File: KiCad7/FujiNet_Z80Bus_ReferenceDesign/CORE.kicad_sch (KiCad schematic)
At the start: 16 parts, among them IC1 74HC32N

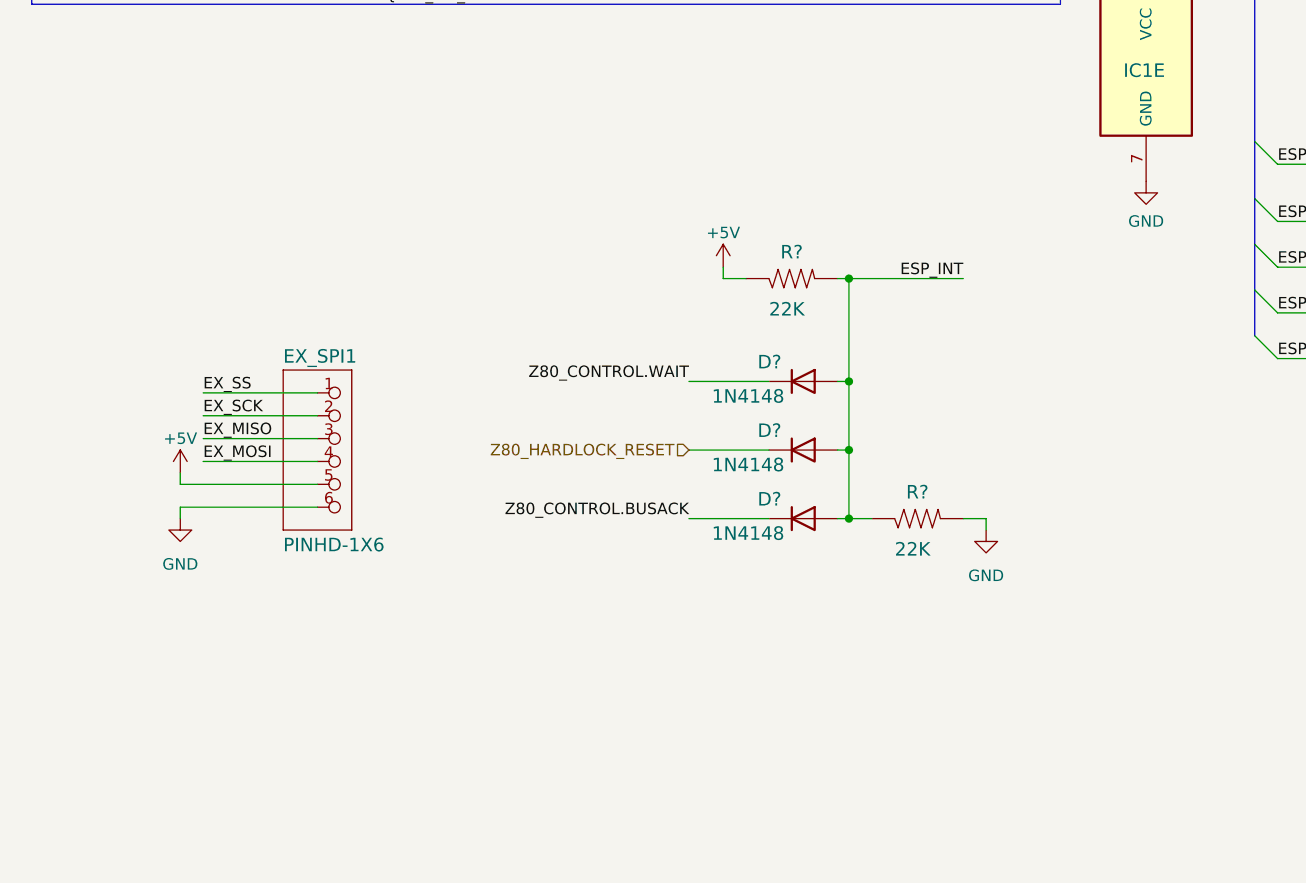
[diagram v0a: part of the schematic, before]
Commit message: KiCad diode OR gate example added to Core
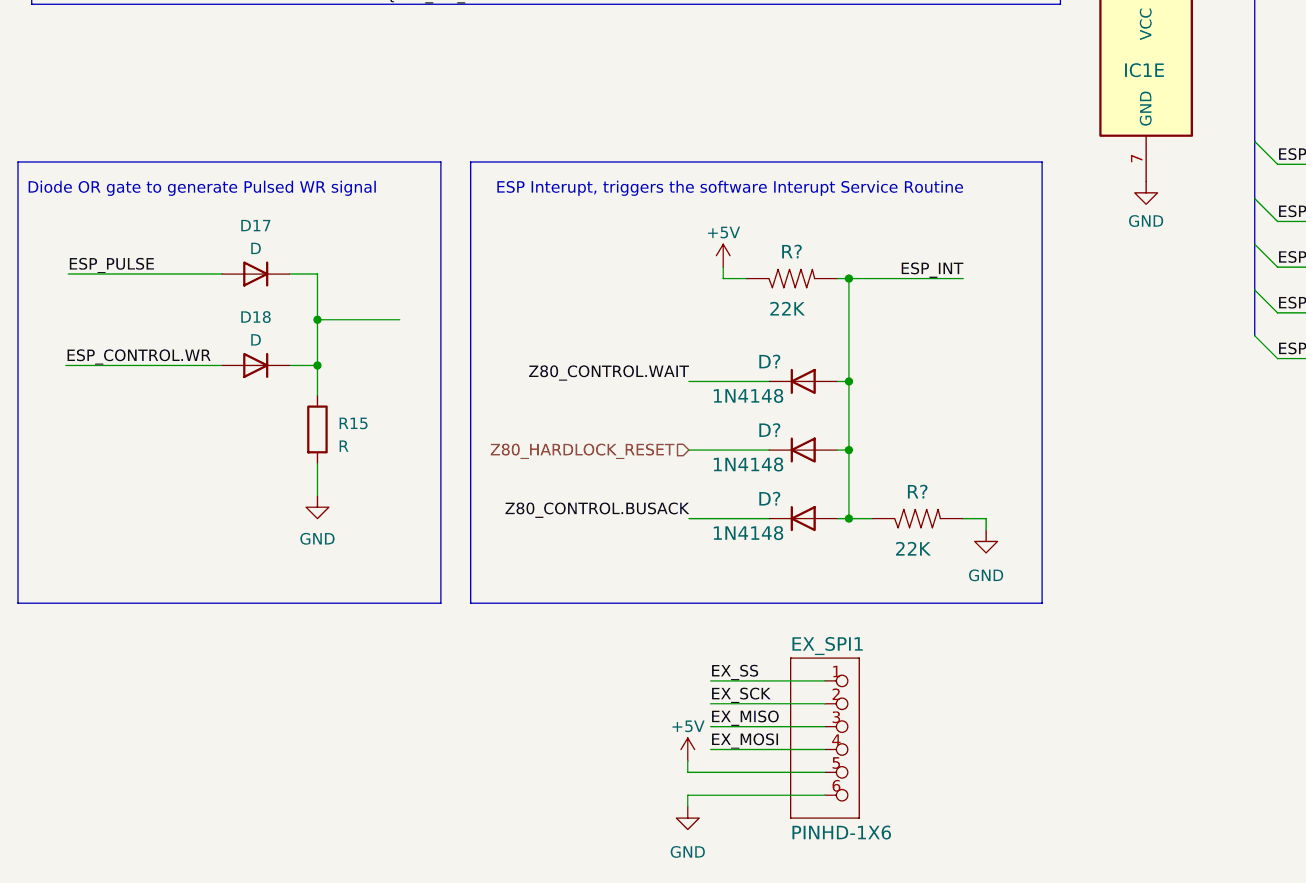
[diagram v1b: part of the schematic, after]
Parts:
- added D17, D18: D, symbol Device:D
- added R15: R, symbol Device:R
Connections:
- net ESP_CONTROL.WR: now also D18.2 (A)
- net ESP_PULSE: now also D17.2 (A)
- net GND: now also R15.2
- new net: D17.1 (K), D18.1 (K), R15.1
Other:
- note added: "Diode OR gate to generate Pulsed WR signal"
- note added: "ESP Interupt, triggers the software Interupt Service Routine"
- moved on the sheet: EX_SPI1

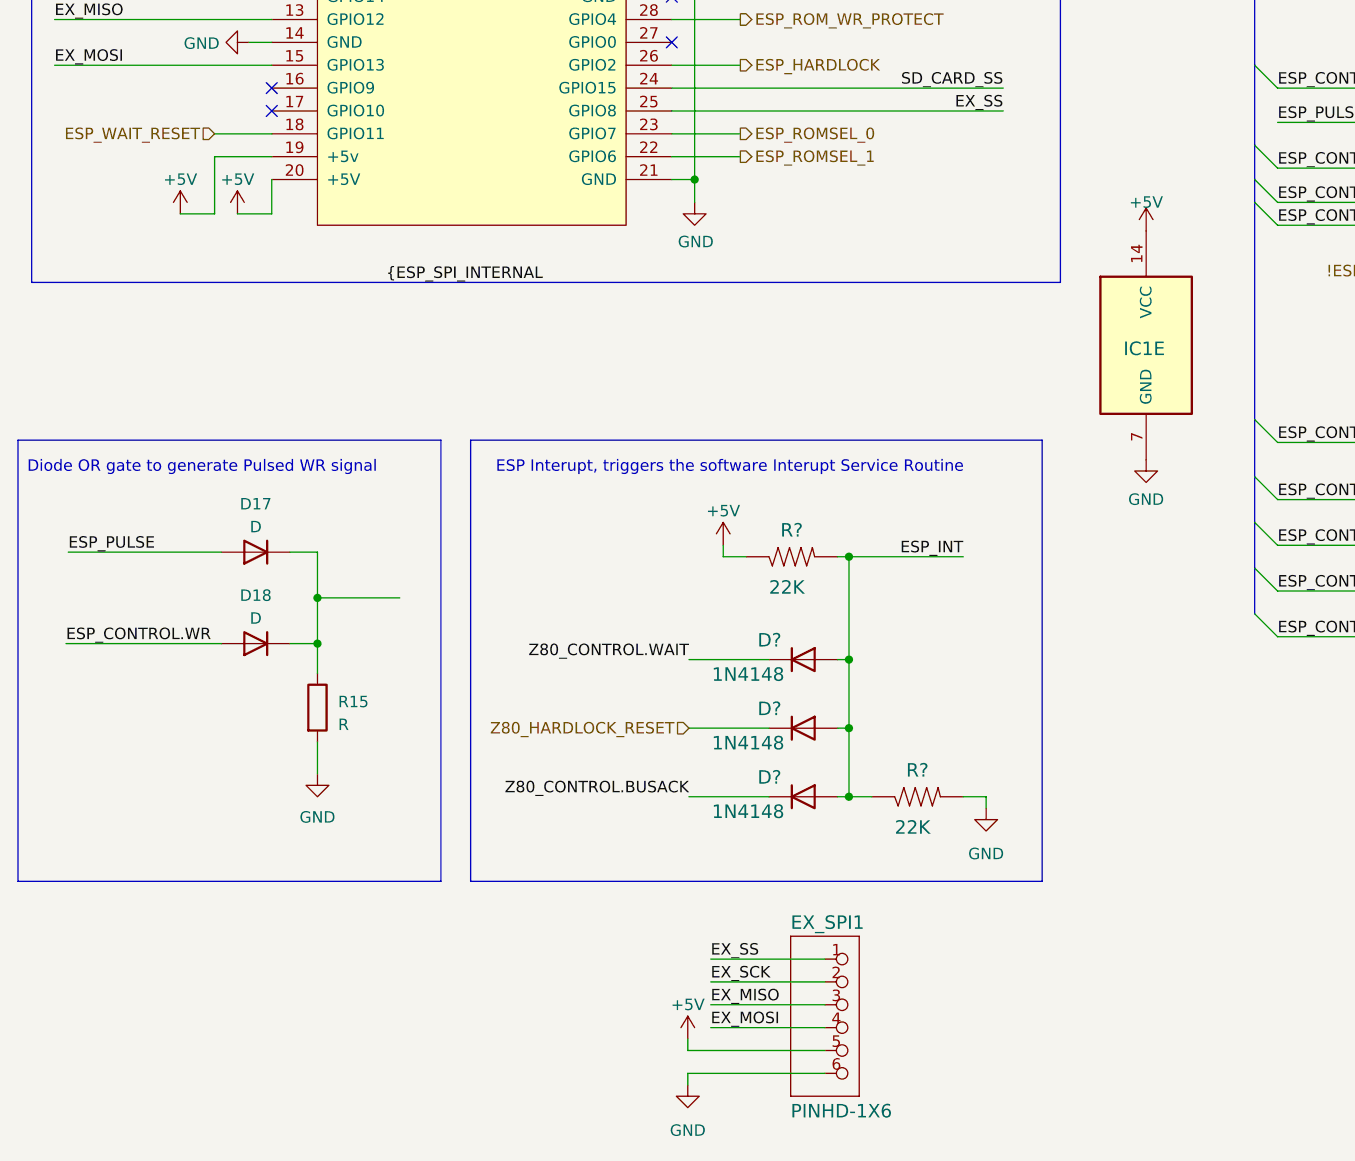
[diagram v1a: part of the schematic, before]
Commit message: KiCad repairing grid alignment
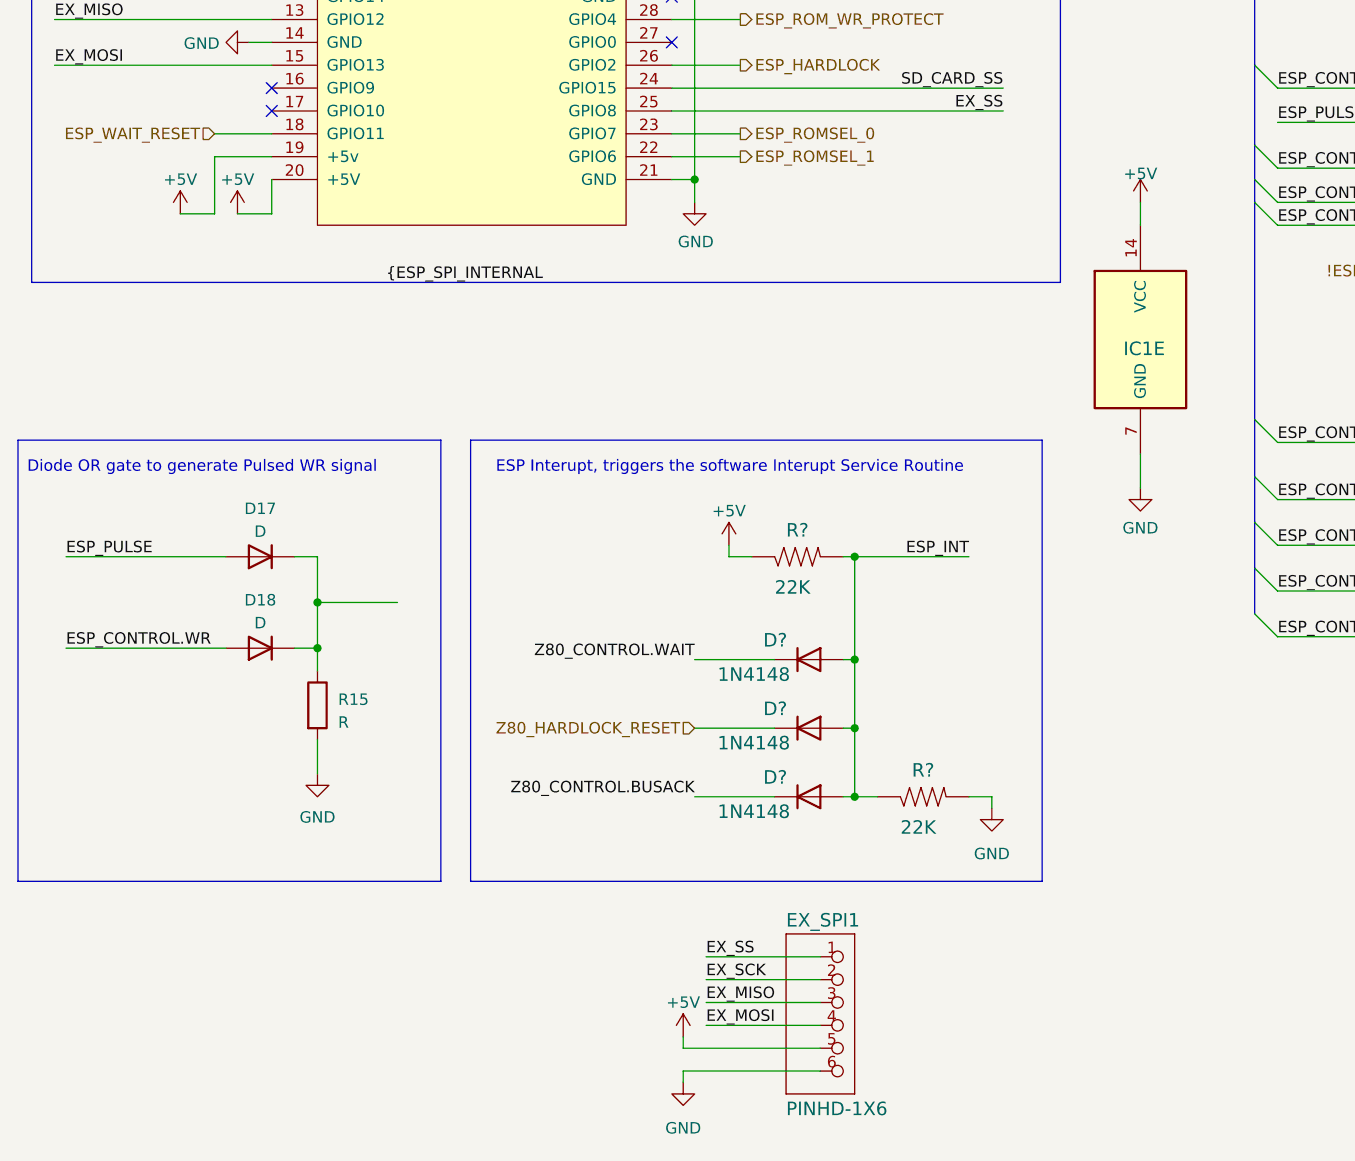
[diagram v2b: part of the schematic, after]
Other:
- moved on the sheet: D17, D18, D?, EX_SPI1, IC1E, R?

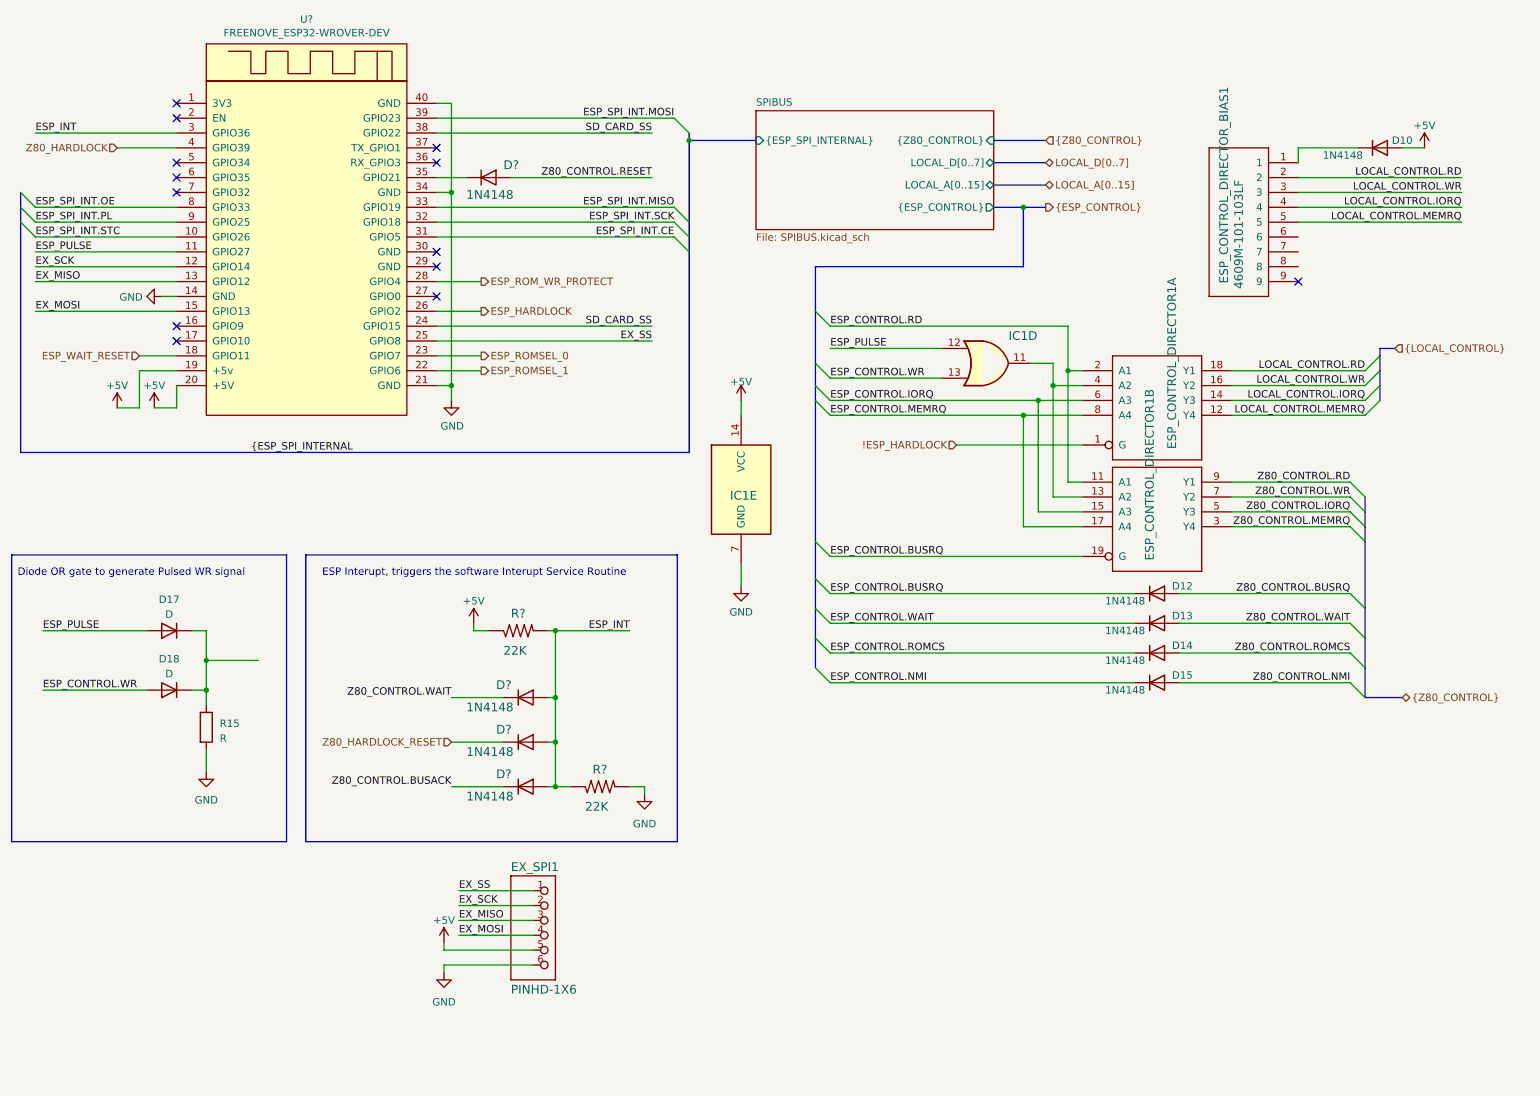
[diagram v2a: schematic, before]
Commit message: KiCAD - grid alignment errors fixed
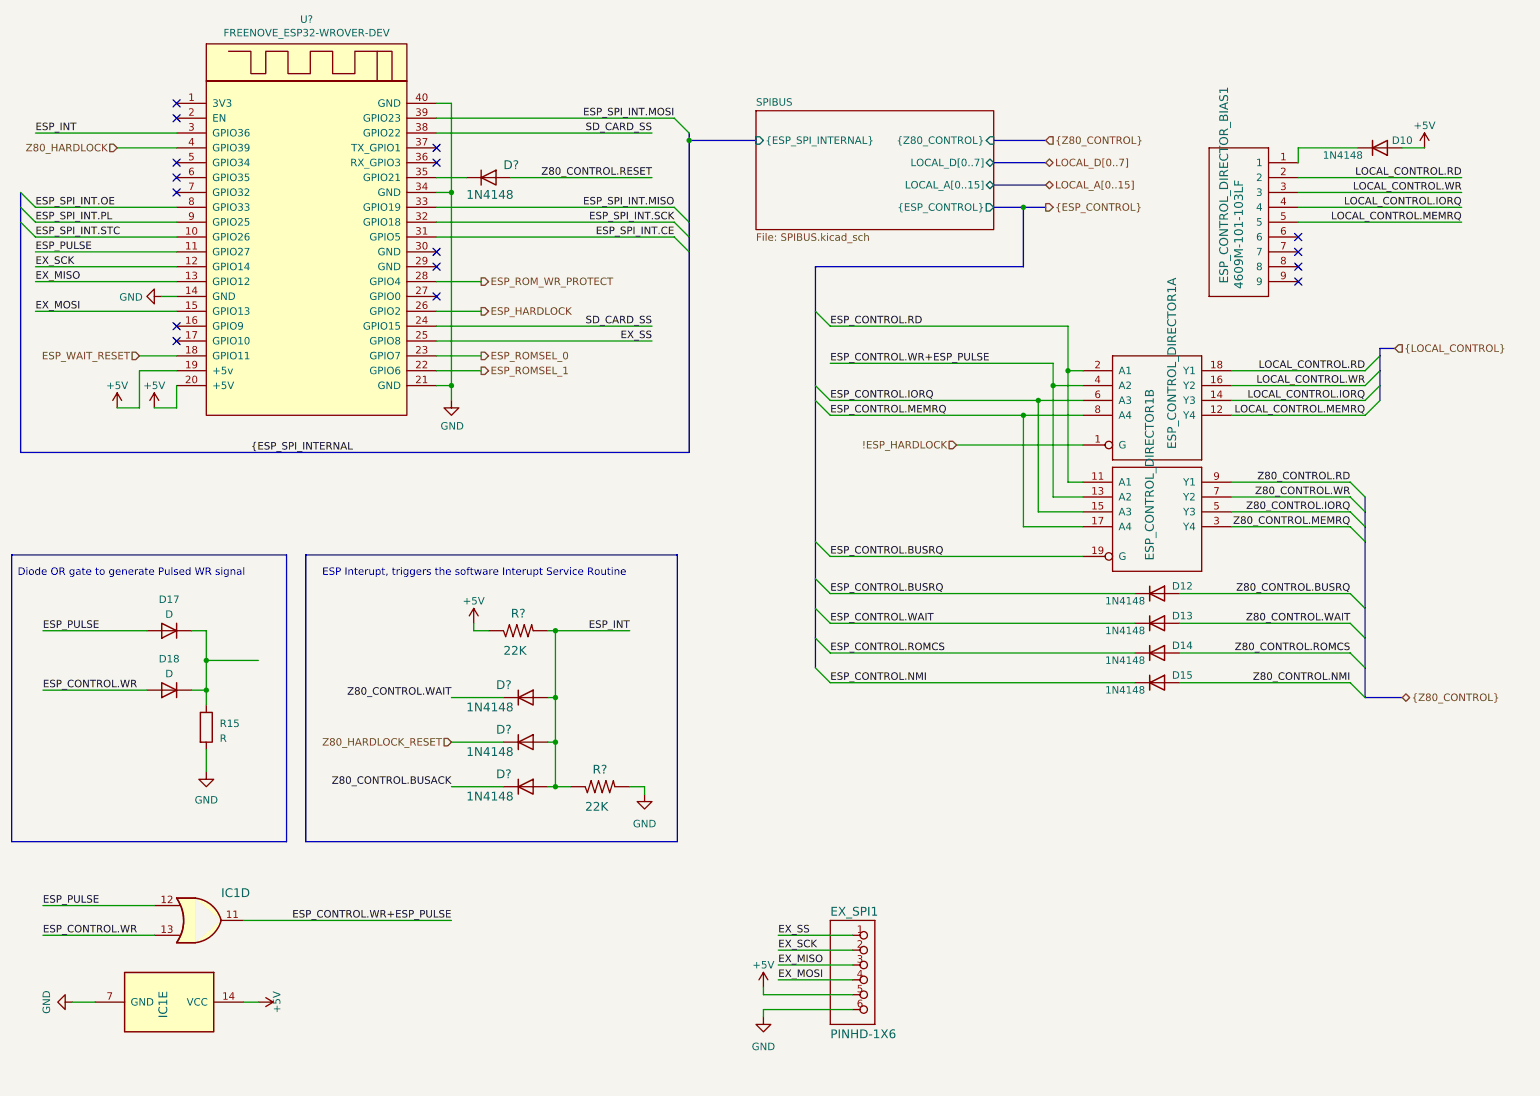
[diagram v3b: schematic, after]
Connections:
- net ESP_CONTROL.WR+ESP_PULSE: now reaches ESP_CONTROL_DIRECTOR1.13 (A2), ESP_CONTROL_DIRECTOR1.4 (A2), IC1.11
- no-connect marks 13 -> 16
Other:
- moved on the sheet: EX_SPI1, IC1E
